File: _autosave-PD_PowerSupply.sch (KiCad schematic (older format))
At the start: 75 parts, among them J1 2.54mm Header, J2 Screw Terminal, Q1 STL6P3LLH6, Q2 STL6P3LLH6, U1 LM1117LD-3.3, U2 STUSB4500QTR, U3 LMR16006YQ5, U4 LTM8074IY, U5 LTC7106EDDB-1, U6 LMP92064SDE_NOPB, U8 BMD-340-A-R, U9 USB6B1

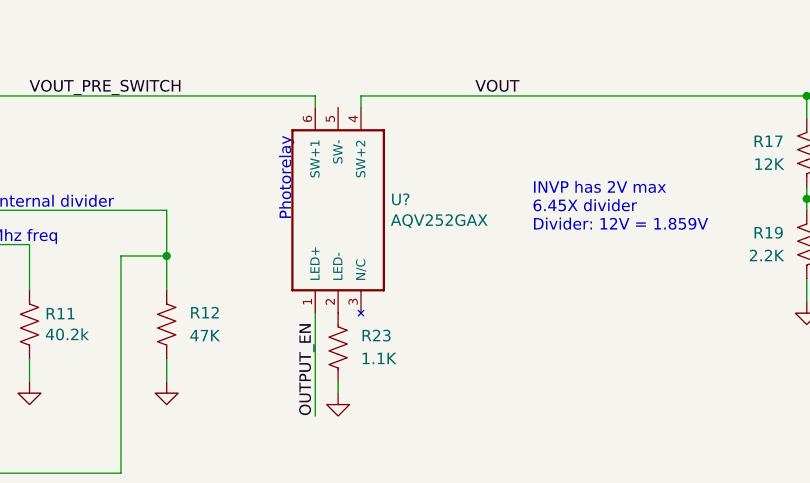
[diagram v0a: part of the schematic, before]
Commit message: Started routing process, swapped out photorelay for an SMD alternative
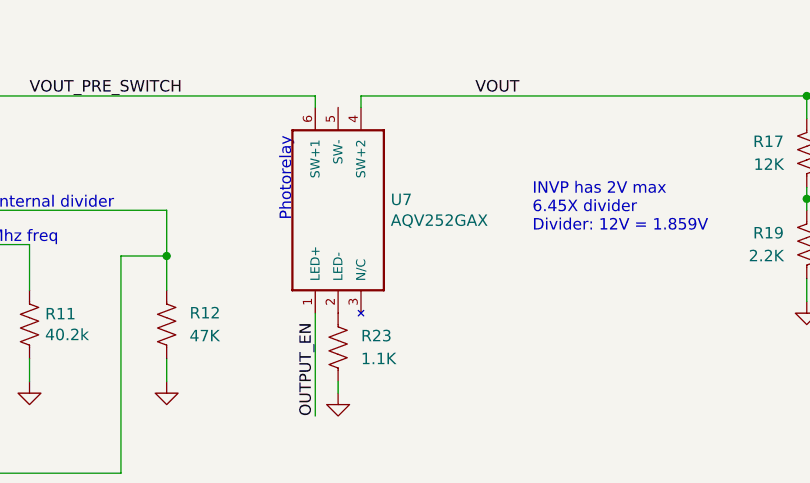
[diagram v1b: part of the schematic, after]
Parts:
- gave numbers to parts that had none: 1
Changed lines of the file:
@@
 	8850 1500 12800 1500
 $Comp
-L AQV252GAX:AQV252GAX U?
+L AQV252GAX:AQV252GAX U7
 U 1 1 5F123B82
 P 17100 1950
-F 0 "U?" V 17096 1720 50  0000 R CNN
+F 0 "U7" V 17096 1720 50  0000 R CNN
 F 1 "AQV252GAX" V 17005 1720 50  0000 R CNN
 F 2 "SOP6" H 17100 1950 50  0001 L BNN
